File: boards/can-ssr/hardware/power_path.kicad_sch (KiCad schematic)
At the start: 24 parts, among them Q1 IPB110N20N3LF, Q2 IPB110N20N3LF, Q3 IPB110N20N3LF, Q4 IPB110N20N3LF, Q5 MMBT2907A, U10 VOM1271T, U11 VOM1271T, U12 ACS770ECB-100U-PFF-T

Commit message: can-ssr schematic: display block; schematic capture complete
- MAX7219CWG+ driving a Kingbright CC56-12SRWA 4-digit red display
  (RSET 27k, ~15 mA peak) plus V/A indicator LEDs on digit 4
- Bolt pads H1-H4 excluded from the BOM
- ERC: 0 violations across all six sheets; every assembled part has
  Manufacturer and MPN

Co-Authored-By: Claude Opus 5.5 <noreply@anthropic.com>
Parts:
- H1, H2, H3, H4: now left out of the parts list
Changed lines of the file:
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@@
 		(unit 1)
 		(exclude_from_sim no)
-		(in_bom yes)
+		(in_bom no)
 		(on_board yes)
 		(dnp no)
@@
 		(instances
 			(project "can-ssr"
-				(path "/09b96810-cbdb-496a-83a0-e49ecf8d36fe/9f2e283d-9951-472b-941a-83d175264942"
+				(path "/09b96810-cbdb-496a-83a0-e49ecf8d36fe/d4795749-164b-4982-89d8-a794ca71454f"
 					(reference "H1")
 					(unit 1)
@@
 		(unit 1)
 		(exclude_from_sim no)
-		(in_bom yes)
+		(in_bom no)
 		(on_board yes)
 		(dnp no)
@@
 		(instances
 			(project "can-ssr"
-				(path "/09b96810-cbdb-496a-83a0-e49ecf8d36fe/9f2e283d-9951-472b-941a-83d175264942"
+				(path "/09b96810-cbdb-496a-83a0-e49ecf8d36fe/d4795749-164b-4982-89d8-a794ca71454f"
 					(reference "H2")
 					(unit 1)
@@
 		(unit 1)
 		(exclude_from_sim no)
-		(in_bom yes)
+		(in_bom no)
 		(on_board yes)
 		(dnp no)
@@
 		(instances
 			(project "can-ssr"
-				(path "/09b96810-cbdb-496a-83a0-e49ecf8d36fe/9f2e283d-9951-472b-941a-83d175264942"
+				(path "/09b96810-cbdb-496a-83a0-e49ecf8d36fe/d4795749-164b-4982-89d8-a794ca71454f"
 					(reference "H3")
 					(unit 1)
@@
 		(unit 1)
 		(exclude_from_sim no)
-		(in_bom yes)
+		(in_bom no)
 		(on_board yes)
 		(dnp no)
@@
 		(instances
 			(project "can-ssr"
-				(path "/09b96810-cbdb-496a-83a0-e49ecf8d36fe/9f2e283d-9951-472b-941a-83d175264942"
+				(path "/09b96810-cbdb-496a-83a0-e49ecf8d36fe/d4795749-164b-4982-89d8-a794ca71454f"
 					(reference "H4")
 					(unit 1)
@@
 		(instances
 			(project "can-ssr"
-				(path "/09b96810-cbdb-496a-83a0-e49ecf8d36fe/9f2e283d-9951-472b-941a-83d175264942"
+				(path "/09b96810-cbdb-496a-83a0-e49ecf8d36fe/d4795749-164b-4982-89d8-a794ca71454f"
 					(reference "Q1")
 					(unit 1)
@@
 		(instances
 			(project "can-ssr"
-				(path "/09b96810-cbdb-496a-83a0-e49ecf8d36fe/9f2e283d-9951-472b-941a-83d175264942"
+				(path "/09b96810-cbdb-496a-83a0-e49ecf8d36fe/d4795749-164b-4982-89d8-a794ca71454f"
 					(reference "Q2")
 					(unit 1)
@@
 		(instances
 			(project "can-ssr"
-				(path "/09b96810-cbdb-496a-83a0-e49ecf8d36fe/9f2e283d-9951-472b-941a-83d175264942"
+				(path "/09b96810-cbdb-496a-83a0-e49ecf8d36fe/d4795749-164b-4982-89d8-a794ca71454f"
 					(reference "Q3")
 					(unit 1)
@@
 		(instances
 			(project "can-ssr"
-				(path "/09b96810-cbdb-496a-83a0-e49ecf8d36fe/9f2e283d-9951-472b-941a-83d175264942"
+				(path "/09b96810-cbdb-496a-83a0-e49ecf8d36fe/d4795749-164b-4982-89d8-a794ca71454f"
 					(reference "Q4")
 					(unit 1)
@@
 		(instances
 			(project "can-ssr"
-				(path "/09b96810-cbdb-496a-83a0-e49ecf8d36fe/9f2e283d-9951-472b-941a-83d175264942"
+				(path "/09b96810-cbdb-496a-83a0-e49ecf8d36fe/d4795749-164b-4982-89d8-a794ca71454f"
 					(reference "R10")
 					(unit 1)
@@
 		(instances
 			(project "can-ssr"
-				(path "/09b96810-cbdb-496a-83a0-e49ecf8d36fe/9f2e283d-9951-472b-941a-83d175264942"
+				(path "/09b96810-cbdb-496a-83a0-e49ecf8d36fe/d4795749-164b-4982-89d8-a794ca71454f"
 					(reference "R11")
 					(unit 1)
@@
 		(instances
 			(project "can-ssr"
-				(path "/09b96810-cbdb-496a-83a0-e49ecf8d36fe/9f2e283d-9951-472b-941a-83d175264942"
+				(path "/09b96810-cbdb-496a-83a0-e49ecf8d36fe/d4795749-164b-4982-89d8-a794ca71454f"
 					(reference "R12")
 					(unit 1)
@@
 		(instances
 			(project "can-ssr"
-				(path "/09b96810-cbdb-496a-83a0-e49ecf8d36fe/9f2e283d-9951-472b-941a-83d175264942"
+				(path "/09b96810-cbdb-496a-83a0-e49ecf8d36fe/d4795749-164b-4982-89d8-a794ca71454f"
 					(reference "R13")
 					(unit 1)
@@
 		(instances
 			(project "can-ssr"
-				(path "/09b96810-cbdb-496a-83a0-e49ecf8d36fe/9f2e283d-9951-472b-941a-83d175264942"
+				(path "/09b96810-cbdb-496a-83a0-e49ecf8d36fe/d4795749-164b-4982-89d8-a794ca71454f"
 					(reference "R14")
 					(unit 1)
@@
 		(instances
 			(project "can-ssr"
-				(path "/09b96810-cbdb-496a-83a0-e49ecf8d36fe/9f2e283d-9951-472b-941a-83d175264942"
+				(path "/09b96810-cbdb-496a-83a0-e49ecf8d36fe/d4795749-164b-4982-89d8-a794ca71454f"
 					(reference "D10")
 					(unit 1)
@@
 		(instances
 			(project "can-ssr"
-				(path "/09b96810-cbdb-496a-83a0-e49ecf8d36fe/9f2e283d-9951-472b-941a-83d175264942"
+				(path "/09b96810-cbdb-496a-83a0-e49ecf8d36fe/d4795749-164b-4982-89d8-a794ca71454f"
 					(reference "D11")
 					(unit 1)
@@
 		(instances
 			(project "can-ssr"
-				(path "/09b96810-cbdb-496a-83a0-e49ecf8d36fe/9f2e283d-9951-472b-941a-83d175264942"
+				(path "/09b96810-cbdb-496a-83a0-e49ecf8d36fe/d4795749-164b-4982-89d8-a794ca71454f"
 					(reference "Q5")
 					(unit 1)
@@
 		(instances
 			(project "can-ssr"
-				(path "/09b96810-cbdb-496a-83a0-e49ecf8d36fe/9f2e283d-9951-472b-941a-83d175264942"
+				(path "/09b96810-cbdb-496a-83a0-e49ecf8d36fe/d4795749-164b-4982-89d8-a794ca71454f"
 					(reference "C10")
 					(unit 1)
@@
 		(instances
 			(project "can-ssr"
-				(path "/09b96810-cbdb-496a-83a0-e49ecf8d36fe/9f2e283d-9951-472b-941a-83d175264942"
+				(path "/09b96810-cbdb-496a-83a0-e49ecf8d36fe/d4795749-164b-4982-89d8-a794ca71454f"
 					(reference "D12")
 					(unit 1)
@@
 		(instances
 			(project "can-ssr"
-				(path "/09b96810-cbdb-496a-83a0-e49ecf8d36fe/9f2e283d-9951-472b-941a-83d175264942"
+				(path "/09b96810-cbdb-496a-83a0-e49ecf8d36fe/d4795749-164b-4982-89d8-a794ca71454f"
 					(reference "R15")
 					(unit 1)
@@
 		(instances
 			(project "can-ssr"
-				(path "/09b96810-cbdb-496a-83a0-e49ecf8d36fe/9f2e283d-9951-472b-941a-83d175264942"
+				(path "/09b96810-cbdb-496a-83a0-e49ecf8d36fe/d4795749-164b-4982-89d8-a794ca71454f"
 					(reference "U10")
 					(unit 1)
@@
 		(instances
 			(project "can-ssr"
-				(path "/09b96810-cbdb-496a-83a0-e49ecf8d36fe/9f2e283d-9951-472b-941a-83d175264942"
+				(path "/09b96810-cbdb-496a-83a0-e49ecf8d36fe/d4795749-164b-4982-89d8-a794ca71454f"
 					(reference "U11")
 					(unit 1)
@@
 		(instances
 			(project "can-ssr"
-				(path "/09b96810-cbdb-496a-83a0-e49ecf8d36fe/9f2e283d-9951-472b-941a-83d175264942"
+				(path "/09b96810-cbdb-496a-83a0-e49ecf8d36fe/d4795749-164b-4982-89d8-a794ca71454f"
 					(reference "U12")
 					(unit 1)
@@
 		(instances
 			(project "can-ssr"
-				(path "/09b96810-cbdb-496a-83a0-e49ecf8d36fe/9f2e283d-9951-472b-941a-83d175264942"
+				(path "/09b96810-cbdb-496a-83a0-e49ecf8d36fe/d4795749-164b-4982-89d8-a794ca71454f"
 					(reference "#PWR01")
 					(unit 1)
@@
 		(instances
 			(project "can-ssr"
-				(path "/09b96810-cbdb-496a-83a0-e49ecf8d36fe/9f2e283d-9951-472b-941a-83d175264942"
+				(path "/09b96810-cbdb-496a-83a0-e49ecf8d36fe/d4795749-164b-4982-89d8-a794ca71454f"
 					(reference "#PWR02")
 					(unit 1)
@@
 		(instances
 			(project "can-ssr"
-				(path "/09b96810-cbdb-496a-83a0-e49ecf8d36fe/9f2e283d-9951-472b-941a-83d175264942"
+				(path "/09b96810-cbdb-496a-83a0-e49ecf8d36fe/d4795749-164b-4982-89d8-a794ca71454f"
 					(reference "C11")
 					(unit 1)
@@
 		(instances
 			(project "can-ssr"
-				(path "/09b96810-cbdb-496a-83a0-e49ecf8d36fe/9f2e283d-9951-472b-941a-83d175264942"
+				(path "/09b96810-cbdb-496a-83a0-e49ecf8d36fe/d4795749-164b-4982-89d8-a794ca71454f"
 					(reference "#PWR03")
 					(unit 1)
@@
 		(instances
 			(project "can-ssr"
-				(path "/09b96810-cbdb-496a-83a0-e49ecf8d36fe/9f2e283d-9951-472b-941a-83d175264942"
+				(path "/09b96810-cbdb-496a-83a0-e49ecf8d36fe/d4795749-164b-4982-89d8-a794ca71454f"
 					(reference "#PWR04")
 					(unit 1)
@@
 		(instances
 			(project "can-ssr"
-				(path "/09b96810-cbdb-496a-83a0-e49ecf8d36fe/9f2e283d-9951-472b-941a-83d175264942"
+				(path "/09b96810-cbdb-496a-83a0-e49ecf8d36fe/d4795749-164b-4982-89d8-a794ca71454f"
 					(reference "D13")
 					(unit 1)

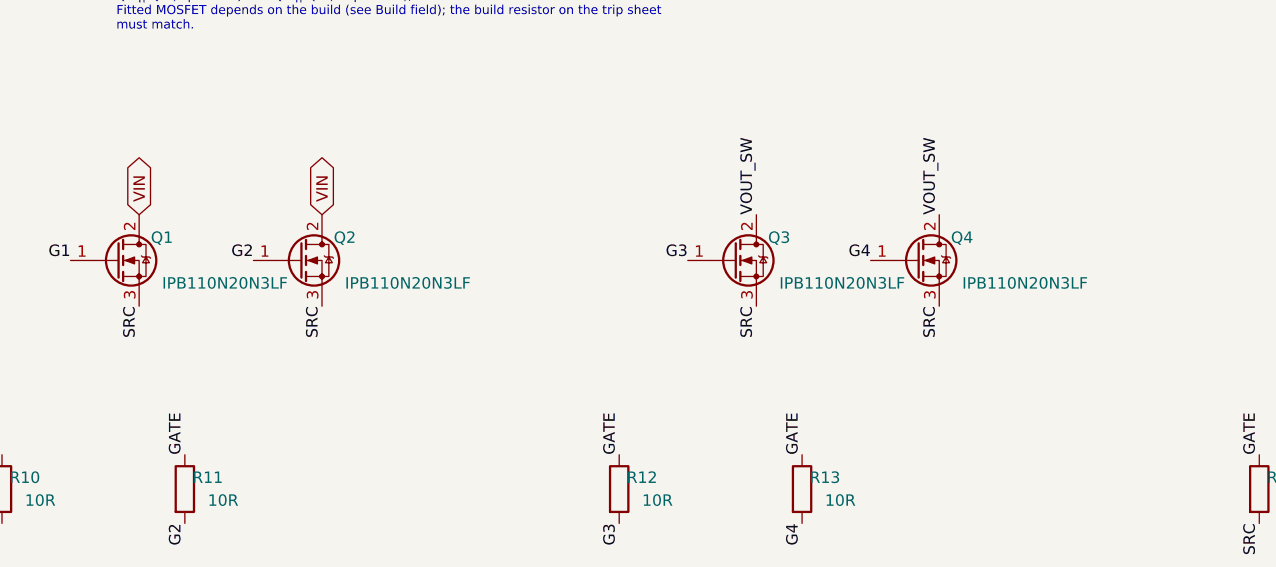
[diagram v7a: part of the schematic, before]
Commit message: can-ssr: STD MOSFET IPB110N20N3LF (discontinued) -> IPB107N20N3G
Infineon's listed successor, same D2PAK footprint, no layout change. It is a
standard OptiMOS 3 without the Linear FET's wide SOA, so STD is now
sequenced-only: firmware 0.3 refuses hot turn-on on STD as on HV. No other
200 V 3-pin D2PAK linear-mode FET fits (IXTA30N25L2 is 140 mOhm).

fab.py: MPN_FIXUPS maps schematic MPNs to orderable DigiKey part numbers
(SH-7010C -> SH-7010MC).

Co-Authored-By: Claude Opus 5.5 <noreply@anthropic.com>
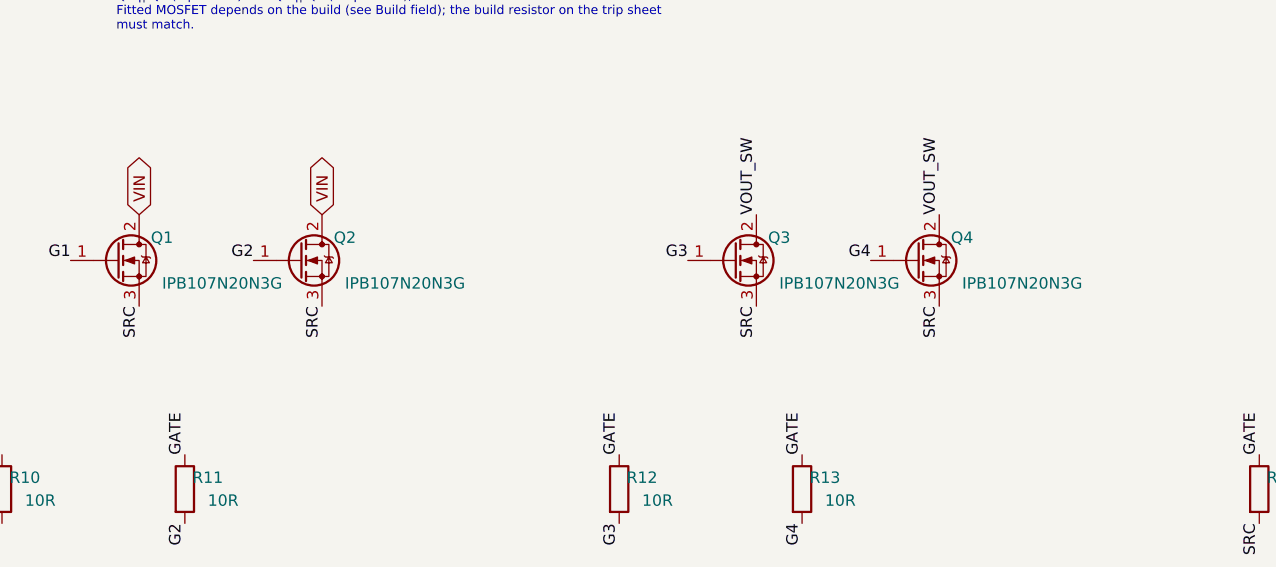
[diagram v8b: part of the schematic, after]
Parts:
- Q1, Q2, Q3, Q4: value IPB110N20N3LF -> IPB107N20N3G; Build HC: IPB021N10NM5LF2 / STD: IPB110N20N3LF / HV: IPB407N30N (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 -> HC: IPB021N10NM5LF2 / STD: IPB107N20N3G / HV: IPB407N30N (a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; MPN IPB110N20N3LFATMA1 -> IPB107N20N3GATMA1
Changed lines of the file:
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@@
 			)
 		)
-		(property "Value" "IPB110N20N3LF"
+		(property "Value" "IPB107N20N3G"
 			(at 101.6 78.74 0)
 			(effects
@@
 			)
 		)
-		(property "MPN" "IPB110N20N3LFATMA1"
-			(at 96.52 76.2 0)
-			(hide yes)
-			(effects
-				(font
-					(size 1.27 1.27)
-				)
-			)
-		)
-		(property "Build" "HC: IPB021N10NM5LF2 / STD: IPB110N20N3LF / HV: IPB407N30N (all Infineon D2PAK)"
+		(property "MPN" "IPB107N20N3GATMA1"
+			(at 96.52 76.2 0)
+			(hide yes)
+			(effects
+				(font
+					(size 1.27 1.27)
+				)
+			)
+		)
+		(property "Build" "HC: IPB021N10NM5LF2 / STD: IPB107N20N3G / HV: IPB407N30N (all Infineon D2PAK)"
 			(at 96.52 76.2 0)
 			(hide yes)
@@
 			)
 		)
-		(property "Value" "IPB110N20N3LF"
+		(property "Value" "IPB107N20N3G"
 			(at 121.92 78.74 0)
 			(effects
@@
 			)
 		)
-		(property "MPN" "IPB110N20N3LFATMA1"
-			(at 116.84 76.2 0)
-			(hide yes)
-			(effects
-				(font
-					(size 1.27 1.27)
-				)
-			)
-		)
-		(property "Build" "HC: IPB021N10NM5LF2 / STD: IPB110N20N3LF / HV: IPB407N30N (all Infineon D2PAK)"
+		(property "MPN" "IPB107N20N3GATMA1"
+			(at 116.84 76.2 0)
+			(hide yes)
+			(effects
+				(font
+					(size 1.27 1.27)
+				)
+			)
+		)
+		(property "Build" "HC: IPB021N10NM5LF2 / STD: IPB107N20N3G / HV: IPB407N30N (all Infineon D2PAK)"
 			(at 116.84 76.2 0)
 			(hide yes)
@@
 			)
 		)
-		(property "Value" "IPB110N20N3LF"
+		(property "Value" "IPB107N20N3G"
 			(at 170.18 78.74 0)
 			(effects
@@
 			)
 		)
-		(property "MPN" "IPB110N20N3LFATMA1"
-			(at 165.1 76.2 0)
-			(hide yes)
-			(effects
-				(font
-					(size 1.27 1.27)
-				)
-			)
-		)
-		(property "Build" "HC: IPB021N10NM5LF2 / STD: IPB110N20N3LF / HV: IPB407N30N (all Infineon D2PAK)"
+		(property "MPN" "IPB107N20N3GATMA1"
+			(at 165.1 76.2 0)
+			(hide yes)
+			(effects
+				(font
+					(size 1.27 1.27)
+				)
+			)
+		)
+		(property "Build" "HC: IPB021N10NM5LF2 / STD: IPB107N20N3G / HV: IPB407N30N (all Infineon D2PAK)"
 			(at 165.1 76.2 0)
 			(hide yes)
@@
 			)
 		)
-		(property "Value" "IPB110N20N3LF"
+		(property "Value" "IPB107N20N3G"
 			(at 190.5 78.74 0)
 			(effects
@@
 			)
 		)
-		(property "MPN" "IPB110N20N3LFATMA1"
-			(at 185.42 76.2 0)
-			(hide yes)
-			(effects
-				(font
-					(size 1.27 1.27)
-				)
-			)
-		)
-		(property "Build" "HC: IPB021N10NM5LF2 / STD: IPB110N20N3LF / HV: IPB407N30N (all Infineon D2PAK)"
-			(at 185.42 76.2 0)
-			(hide yes)
+		(property "MPN" "IPB107N20N3GATMA1"
+			(at 185.42 76.2 0)
+			(hide yes)
+			(effects
+				(font
+					(size 1.27 1.27)
+				)
+			)
+		)
+		(property "Build" "HC: IPB021N10NM5LF2 / STD: IPB107N20N3G / HV: IPB407N30N (all Infineon D2PAK)"
+			(at 185.42 76.2 0)
+			(hide yes)
